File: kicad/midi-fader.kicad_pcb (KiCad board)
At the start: 2 copper layers, 73.7 x 78.7 mm, 94 parts, among them J1 SWD, J2 EXTERNAL_OUT, J3 EXTERNAL_IN, J4 USB_OTG, U1 STM32F042KxT, U2 USBLC6-2, U3 MCP1603, U4 MIC2776L, U5 MIC5501-XYM5

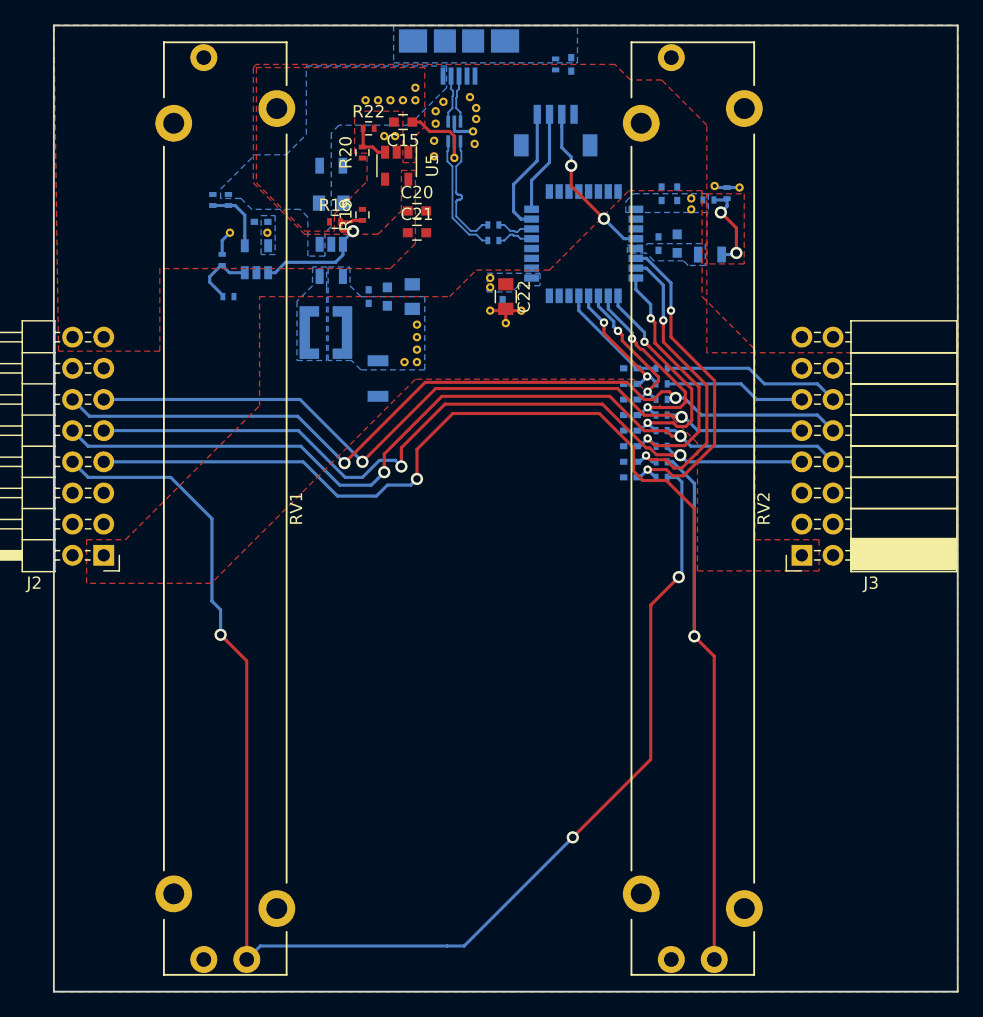
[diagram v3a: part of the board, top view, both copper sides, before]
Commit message: Added corner grounded mounting holes
At the moment I plan on actually attaching the cover using the M2 screw
holes on the sliders themselves, but this seems like a good backup
option to have.
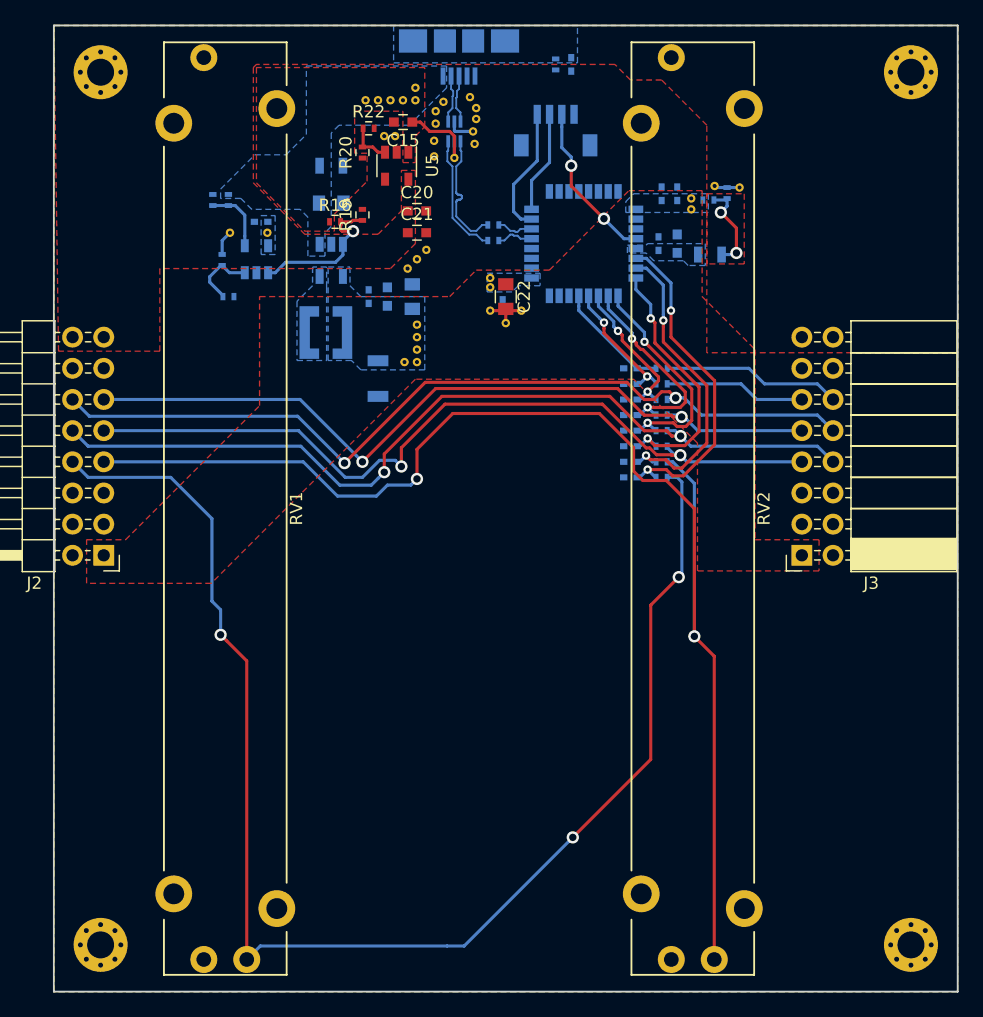
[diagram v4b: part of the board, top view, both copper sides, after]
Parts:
- added REF**: MountingHole_2.2mm_M2_Pad_Via, Mounting_Holes:MountingHole_2.2mm_M2_Pad_Via, F.Cu at (120.7, 138.4)
- added REF**: MountingHole_2.2mm_M2_Pad_Via, Mounting_Holes:MountingHole_2.2mm_M2_Pad_Via, F.Cu at (186.7, 138.4)
- added REF**: MountingHole_2.2mm_M2_Pad_Via, Mounting_Holes:MountingHole_2.2mm_M2_Pad_Via, F.Cu at (186.7, 67.3)
- added REF**: 1PIN_VIA, midi-fader:1PIN_VIA, F.Cu at (145.7, 83.3)
- added REF**: MountingHole_2.2mm_M2_Pad_Via, Mounting_Holes:MountingHole_2.2mm_M2_Pad_Via, F.Cu at (120.7, 67.3)
- added REF**: 1PIN_VIA, midi-fader:1PIN_VIA, F.Cu at (146.4, 82.5)
- added REF**: 1PIN_VIA, midi-fader:1PIN_VIA, F.Cu at (147.2, 81.8)
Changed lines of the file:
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@@
 (kicad_pcb (version 4) (host pcbnew 4.0.7)
   (general
-    (links 175)
+    (links 0)
     (no_connects 3)
     (area 116.764999 63.424999 190.575001 142.315001)
@@
     (tracks 413)
     (zones 0)
-    (modules 94)
+    (modules 101)
     (nets 64)
   )
@@
     (mod_text_size 1 1)
     (mod_text_width 0.15)
-    (pad_size 0.6858 0.6858)
-    (pad_drill 0.3302)
+    (pad_size 0.7 0.7)
+    (pad_drill 0.4)
     (pad_to_mask_clearance 0.1524)
     (aux_axis_origin 0 0)
@@
     (add_net "/Digital Control/USB_TVS_D-")
   )
+  (module Mounting_Holes:MountingHole_2.2mm_M2_Pad_Via (layer F.Cu)
+    (at 120.65 138.43)
+    (descr "Mounting Hole 2.2mm, M2")
+    (tags "mounting hole 2.2mm m2")
+    (attr virtual)
+    (fp_text reference REF** (at 0 -3.2) (layer F.SilkS) hide
+      (effects (font (size 1 1) (thickness 0.15)))
+    )
+    (fp_text value MountingHole_2.2mm_M2_Pad_Via (at 0 3.2) (layer F.Fab)
+      (effects (font (size 1 1) (thickness 0.15)))
+    )
+    (fp_text user %R (at 0.3 0) (layer F.Fab)
+      (effects (font (size 1 1) (thickness 0.15)))
+    )
+    (fp_circle (center 0 0) (end 2.2 0) (layer Cmts.User) (width 0.15))
+    (fp_circle (center 0 0) (end 2.45 0) (layer F.CrtYd) (width 0.05))
+    (pad 1 thru_hole circle (at 0 0) (size 4.4 4.4) (drill 2.2) (layers *.Cu *.Mask)
+      (net 2 GND))
+    (pad 1 thru_hole circle (at 1.65 0) (size 0.7 0.7) (drill 0.4) (layers *.Cu *.Mask)
+      (net 2 GND))
+    (pad 1 thru_hole circle (at 1.166726 1.166726) (size 0.7 0.7) (drill 0.4) (layers *.Cu *.Mask)
+      (net 2 GND))
+    (pad 1 thru_hole circle (at 0 1.65) (size 0.7 0.7) (drill 0.4) (layers *.Cu *.Mask)
+      (net 2 GND))
+    (pad 1 thru_hole circle (at -1.166726 1.166726) (size 0.7 0.7) (drill 0.4) (layers *.Cu *.Mask)
+      (net 2 GND))
+    (pad 1 thru_hole circle (at -1.65 0) (size 0.7 0.7) (drill 0.4) (layers *.Cu *.Mask)
+      (net 2 GND))
+    (pad 1 thru_hole circle (at -1.166726 -1.166726) (size 0.7 0.7) (drill 0.4) (layers *.Cu *.Mask)
+      (net 2 GND))
+    (pad 1 thru_hole circle (at 0 -1.65) (size 0.7 0.7) (drill 0.4) (layers *.Cu *.Mask)
+      (net 2 GND))
+    (pad 1 thru_hole circle (at 1.166726 -1.166726) (size 0.7 0.7) (drill 0.4) (layers *.Cu *.Mask)
+      (net 2 GND))
+  )
+  (module Mounting_Holes:MountingHole_2.2mm_M2_Pad_Via (layer F.Cu)
+    (at 186.69 138.43)
+    (descr "Mounting Hole 2.2mm, M2")
+    (tags "mounting hole 2.2mm m2")
+    (attr virtual)
+    (fp_text reference REF** (at 0 -3.2) (layer F.SilkS) hide
+      (effects (font (size 1 1) (thickness 0.15)))
+    )
+    (fp_text value MountingHole_2.2mm_M2_Pad_Via (at 0 3.2) (layer F.Fab)
+      (effects (font (size 1 1) (thickness 0.15)))
+    )
+    (fp_text user %R (at 0.3 0) (layer F.Fab)
+      (effects (font (size 1 1) (thickness 0.15)))
+    )
+    (fp_circle (center 0 0) (end 2.2 0) (layer Cmts.User) (width 0.15))
+    (fp_circle (center 0 0) (end 2.45 0) (layer F.CrtYd) (width 0.05))
+    (pad 1 thru_hole circle (at 0 0) (size 4.4 4.4) (drill 2.2) (layers *.Cu *.Mask)
+      (net 2 GND))
+    (pad 1 thru_hole circle (at 1.65 0) (size 0.7 0.7) (drill 0.4) (layers *.Cu *.Mask)
+      (net 2 GND))
+    (pad 1 thru_hole circle (at 1.166726 1.166726) (size 0.7 0.7) (drill 0.4) (layers *.Cu *.Mask)
+      (net 2 GND))
+    (pad 1 thru_hole circle (at 0 1.65) (size 0.7 0.7) (drill 0.4) (layers *.Cu *.Mask)
+      (net 2 GND))
+    (pad 1 thru_hole circle (at -1.166726 1.166726) (size 0.7 0.7) (drill 0.4) (layers *.Cu *.Mask)
+      (net 2 GND))
+    (pad 1 thru_hole circle (at -1.65 0) (size 0.7 0.7) (drill 0.4) (layers *.Cu *.Mask)
+      (net 2 GND))
+    (pad 1 thru_hole circle (at -1.166726 -1.166726) (size 0.7 0.7) (drill 0.4) (layers *.Cu *.Mask)
+      (net 2 GND))
+    (pad 1 thru_hole circle (at 0 -1.65) (size 0.7 0.7) (drill 0.4) (layers *.Cu *.Mask)
+      (net 2 GND))
+    (pad 1 thru_hole circle (at 1.166726 -1.166726) (size 0.7 0.7) (drill 0.4) (layers *.Cu *.Mask)
+      (net 2 GND))
+  )
+  (module Mounting_Holes:MountingHole_2.2mm_M2_Pad_Via (layer F.Cu)
+    (at 186.69 67.31)
+    (descr "Mounting Hole 2.2mm, M2")
+    (tags "mounting hole 2.2mm m2")
+    (attr virtual)
+    (fp_text reference REF** (at 0 -3.2) (layer F.SilkS) hide
+      (effects (font (size 1 1) (thickness 0.15)))
+    )
+    (fp_text value MountingHole_2.2mm_M2_Pad_Via (at 0 3.2) (layer F.Fab)
+      (effects (font (size 1 1) (thickness 0.15)))
+    )
+    (fp_text user %R (at 0.3 0) (layer F.Fab)
+      (effects (font (size 1 1) (thickness 0.15)))
+    )
+    (fp_circle (center 0 0) (end 2.2 0) (layer Cmts.User) (width 0.15))
+    (fp_circle (center 0 0) (end 2.45 0) (layer F.CrtYd) (width 0.05))
+    (pad 1 thru_hole circle (at 0 0) (size 4.4 4.4) (drill 2.2) (layers *.Cu *.Mask)
+      (net 2 GND))
+    (pad 1 thru_hole circle (at 1.65 0) (size 0.7 0.7) (drill 0.4) (layers *.Cu *.Mask)
+      (net 2 GND))
+    (pad 1 thru_hole circle (at 1.166726 1.166726) (size 0.7 0.7) (drill 0.4) (layers *.Cu *.Mask)
+      (net 2 GND))
+    (pad 1 thru_hole circle (at 0 1.65) (size 0.7 0.7) (drill 0.4) (layers *.Cu *.Mask)
+      (net 2 GND))
+    (pad 1 thru_hole circle (at -1.166726 1.166726) (size 0.7 0.7) (drill 0.4) (layers *.Cu *.Mask)
+      (net 2 GND))
+    (pad 1 thru_hole circle (at -1.65 0) (size 0.7 0.7) (drill 0.4) (layers *.Cu *.Mask)
+      (net 2 GND))
+    (pad 1 thru_hole circle (at -1.166726 -1.166726) (size 0.7 0.7) (drill 0.4) (layers *.Cu *.Mask)
+      (net 2 GND))
+    (pad 1 thru_hole circle (at 0 -1.65) (size 0.7 0.7) (drill 0.4) (layers *.Cu *.Mask)
+      (net 2 GND))
+    (pad 1 thru_hole circle (at 1.166726 -1.166726) (size 0.7 0.7) (drill 0.4) (layers *.Cu *.Mask)
+      (net 2 GND))
+  )
+  (module midi-fader:1PIN_VIA (layer F.Cu)
+    (at 145.669 83.312)
+    (fp_text reference REF** (at 0 2) (layer F.SilkS) hide
+      (effects (font (size 1 1) (thickness 0.15)))
+    )
+    (fp_text value 1PIN_VIA (at 0 -2) (layer F.Fab) hide
+      (effects (font (size 1 1) (thickness 0.15)))
+    )
+    (pad 1 thru_hole circle (at 0 0) (size 0.6858 0.6858) (drill 0.3302) (layers *.Cu)
+      (net 2 GND) (zone_connect 2))
+  )
+  (module midi-fader:1PIN_VIA (layer F.Cu)
+    (at 146.431 82.55)
+    (fp_text reference REF** (at 0 2) (layer F.SilkS) hide
+      (effects (font (size 1 1) (thickness 0.15)))
+    )
+    (fp_text value 1PIN_VIA (at 0 -2) (layer F.Fab) hide
+      (effects (font (size 1 1) (thickness 0.15)))
+    )
+    (pad 1 thru_hole circle (at 0 0) (size 0.6858 0.6858) (drill 0.3302) (layers *.Cu)
+      (net 2 GND) (zone_connect 2))
+  )
+  (module midi-fader:1PIN_VIA (layer F.Cu)
+    (at 147.193 81.788)
+    (fp_text reference REF** (at 0 2) (layer F.SilkS) hide
+      (effects (font (size 1 1) (thickness 0.15)))
+    )
+    (fp_text value 1PIN_VIA (at 0 -2) (layer F.Fab) hide
+      (effects (font (size 1 1) (thickness 0.15)))
+    )
+    (pad 1 thru_hole circle (at 0 0) (size 0.6858 0.6858) (drill 0.3302) (layers *.Cu)
+      (net 2 GND) (zone_connect 2))
+  )
   (module midi-fader:1PIN_VIA (layer F.Cu)
     (at 168.783 77.597)
@@
       (net 11 VBUS) (zone_connect 2))
   )
+  (module Mounting_Holes:MountingHole_2.2mm_M2_Pad_Via (layer F.Cu)
+    (at 120.65 67.31)
+    (descr "Mounting Hole 2.2mm, M2")
+    (tags "mounting hole 2.2mm m2")
+    (attr virtual)
+    (fp_text reference REF** (at 0 -3.2) (layer F.SilkS) hide
+      (effects (font (size 1 1) (thickness 0.15)))
+    )
+    (fp_text value MountingHole_2.2mm_M2_Pad_Via (at 0 3.2) (layer F.Fab)
+      (effects (font (size 1 1) (thickness 0.15)))
+    )
+    (fp_text user %R (at 0.3 0) (layer F.Fab)
+      (effects (font (size 1 1) (thickness 0.15)))
+    )
+    (fp_circle (center 0 0) (end 2.2 0) (layer Cmts.User) (width 0.15))
+    (fp_circle (center 0 0) (end 2.45 0) (layer F.CrtYd) (width 0.05))
+    (pad 1 thru_hole circle (at 0 0) (size 4.4 4.4) (drill 2.2) (layers *.Cu *.Mask)
+      (net 2 GND))
+    (pad 1 thru_hole circle (at 1.65 0) (size 0.7 0.7) (drill 0.4) (layers *.Cu *.Mask)
+      (net 2 GND))
+    (pad 1 thru_hole circle (at 1.166726 1.166726) (size 0.7 0.7) (drill 0.4) (layers *.Cu *.Mask)
+      (net 2 GND))
+    (pad 1 thru_hole circle (at 0 1.65) (size 0.7 0.7) (drill 0.4) (layers *.Cu *.Mask)
+      (net 2 GND))
+    (pad 1 thru_hole circle (at -1.166726 1.166726) (size 0.7 0.7) (drill 0.4) (layers *.Cu *.Mask)
+      (net 2 GND))
+    (pad 1 thru_hole circle (at -1.65 0) (size 0.7 0.7) (drill 0.4) (layers *.Cu *.Mask)
+      (net 2 GND))
+    (pad 1 thru_hole circle (at -1.166726 -1.166726) (size 0.7 0.7) (drill 0.4) (layers *.Cu *.Mask)
+      (net 2 GND))
+    (pad 1 thru_hole circle (at 0 -1.65) (size 0.7 0.7) (drill 0.4) (layers *.Cu *.Mask)
+      (net 2 GND))
+    (pad 1 thru_hole circle (at 1.166726 -1.166726) (size 0.7 0.7) (drill 0.4) (layers *.Cu *.Mask)
+      (net 2 GND))
+  )
   (dimension 11.43 (width 0.3) (layer Dwgs.User)

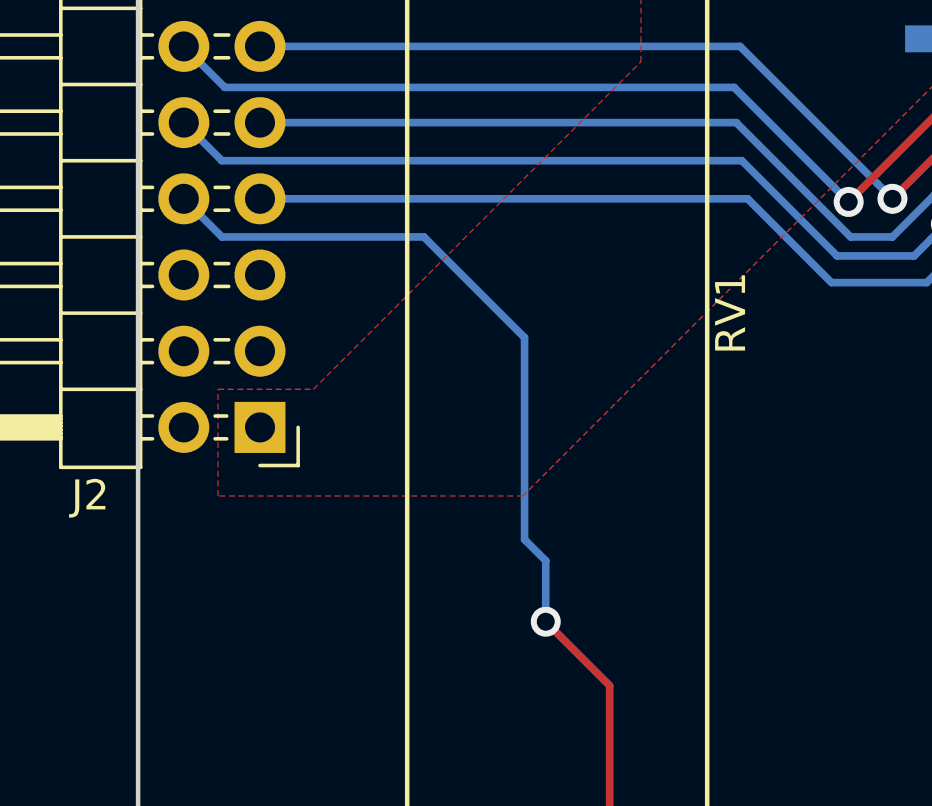
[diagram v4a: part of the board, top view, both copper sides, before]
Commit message: Restructured schematic to have a separate input page
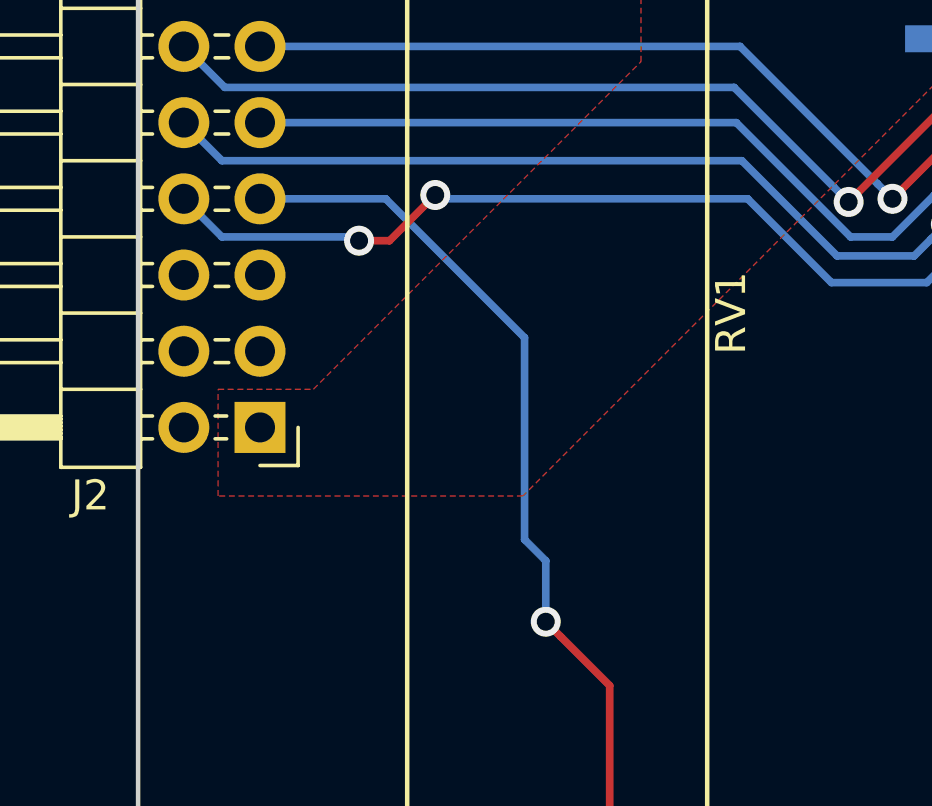
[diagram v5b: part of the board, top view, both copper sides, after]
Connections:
- J2 pad 7: /Digital Control/FADER_B -> /Digital Control/FADER_A
- J2 pad 8: /Digital Control/FADER_A -> /Digital Control/FADER_B
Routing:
- net /Digital Control/FADER_B: track 110.6 -> 114.4 mm, vias 2 -> 4
- net /Digital Control/FADER_A: track 115.1 -> 112.5 mm
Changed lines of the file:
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@@
 (kicad_pcb (version 4) (host pcbnew 4.0.7)
   (general
-    (links 0)
-    (no_connects 3)
+    (links 214)
+    (no_connects 2)
     (area 116.764999 63.424999 190.575001 142.315001)
     (thickness 1.6)
     (drawings 9)
-    (tracks 413)
+    (tracks 420)
     (zones 0)
     (modules 101)
@@
       (net 19 "Net-(J2-Pad6)"))
     (pad 7 thru_hole oval (at 0 7.62 180) (size 1.7 1.7) (drill 1) (layers *.Cu *.Mask)
-      (net 20 "/Digital Control/FADER_B"))
-    (pad 8 thru_hole oval (at 2.54 7.62 180) (size 1.7 1.7) (drill 1) (layers *.Cu *.Mask)
       (net 21 "/Digital Control/FADER_A"))
+    (pad 8 thru_hole oval (at 2.54 7.62 180) (size 1.7 1.7) (drill 1) (layers *.Cu *.Mask)
+      (net 20 "/Digital Control/FADER_B"))
     (pad 9 thru_hole oval (at 0 10.16 180) (size 1.7 1.7) (drill 1) (layers *.Cu *.Mask)
       (net 22 "/Digital Control/IN0"))
@@
   (segment (start 163.303 80.88) (end 161.671 79.248) (width 0.254) (layer B.Cu) (net 15))
   (via (at 161.671 79.248) (size 1) (drill 0.6) (layers F.Cu B.Cu) (net 15))
+  (segment (start 124.206 100.457) (end 124.079 100.33) (width 0.254) (layer B.Cu) (net 20))
+  (segment (start 124.079 100.33) (end 119.634 100.33) (width 0.254) (layer B.Cu) (net 20))
+  (segment (start 119.634 100.33) (end 118.364 99.06) (width 0.254) (layer B.Cu) (net 20))
+  (segment (start 126.746 98.933) (end 125.222 100.457) (width 0.254) (layer F.Cu) (net 20))
+  (via (at 124.206 100.457) (size 1) (drill 0.6) (layers F.Cu B.Cu) (net 20))
+  (segment (start 125.222 100.457) (end 124.206 100.457) (width 0.254) (layer F.Cu) (net 20))
+  (segment (start 137.16 99.06) (end 126.873 99.06) (width 0.254) (layer B.Cu) (net 20))
+  (segment (start 126.873 99.06) (end 126.746 98.933) (width 0.254) (layer B.Cu) (net 20))
+  (via (at 126.746 98.933) (size 1) (drill 0.6) (layers F.Cu B.Cu) (net 20))
   (segment (start 146.431 100.457) (end 145.931001 100.956999) (width 0.254) (layer B.Cu) (net 20))
   (segment (start 145.931001 100.956999) (end 144.026001 100.956999) (width 0.254) (layer B.Cu) (net 20))
@@
   (segment (start 143.129 101.854) (end 139.954 101.854) (width 0.254) (layer B.Cu) (net 20))
   (segment (start 139.954 101.854) (end 137.16 99.06) (width 0.254) (layer B.Cu) (net 20))
-  (segment (start 137.16 99.06) (end 120.904 99.06) (width 0.254) (layer B.Cu) (net 20))
   (segment (start 146.431 98.044) (end 146.431 100.457) (width 0.254) (layer F.Cu) (net 20))
   (via (at 146.431 100.457) (size 1) (drill 0.6) (layers F.Cu B.Cu) (net 20))
@@
   (segment (start 170.66 114.907) (end 169.037 113.284) (width 0.254) (layer F.Cu) (net 20))
   (via (at 169.037 113.284) (size 1) (drill 0.6) (layers F.Cu B.Cu) (net 20))
-  (segment (start 118.364 99.06) (end 119.634 100.33) (width 0.254) (layer B.Cu) (net 21))
-  (segment (start 119.634 100.33) (end 126.365 100.33) (width 0.254) (layer B.Cu) (net 21))
-  (segment (start 126.365 100.33) (end 129.721894 103.686894) (width 0.254) (layer B.Cu) (net 21))
-  (segment (start 129.721894 103.686894) (end 129.721894 110.417894) (width 0.254) (layer B.Cu) (net 21))
-  (segment (start 129.721894 110.417894) (end 130.429 111.125) (width 0.254) (layer B.Cu) (net 21))
-  (segment (start 130.429 111.125) (end 130.429 113.157002) (width 0.254) (layer B.Cu) (net 21))
+  (segment (start 130.429 113.157002) (end 130.429 111.125) (width 0.254) (layer B.Cu) (net 21))
+  (segment (start 125.095 99.06) (end 120.904 99.06) (width 0.254) (layer B.Cu) (net 21))
+  (segment (start 130.429 111.125) (end 129.721894 110.417894) (width 0.254) (layer B.Cu) (net 21))
+  (segment (start 129.721894 110.417894) (end 129.721894 103.686894) (width 0.254) (layer B.Cu) (net 21))
+  (segment (start 129.721894 103.686894) (end 125.095 99.06) (width 0.254) (layer B.Cu) (net 21))
   (segment (start 130.928999 113.657001) (end 130.429 113.157002) (width 0.254) (layer F.Cu) (net 21))
   (segment (start 132.56 115.288002) (end 130.928999 113.657001) (width 0.254) (layer F.Cu) (net 21))
